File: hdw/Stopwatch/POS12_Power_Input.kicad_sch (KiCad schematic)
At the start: 19 parts, among them J201 +12V IN, U201 TPS26600RHFT

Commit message: started sch work
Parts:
- removed C202: 10nF, Capacitors_SMD:C_0603, symbol Custom_Library:C_Custom
- removed C203: 1nF, Capacitors_SMD:C_0603, symbol Custom_Library:C_Custom
- D201: Config (none) -> DNP
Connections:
- net at U201.12 (OVP): now also R?.1, R?.2
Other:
- moved on the sheet: C201, C204, C205, D201, J201, R?, TP201, TP203

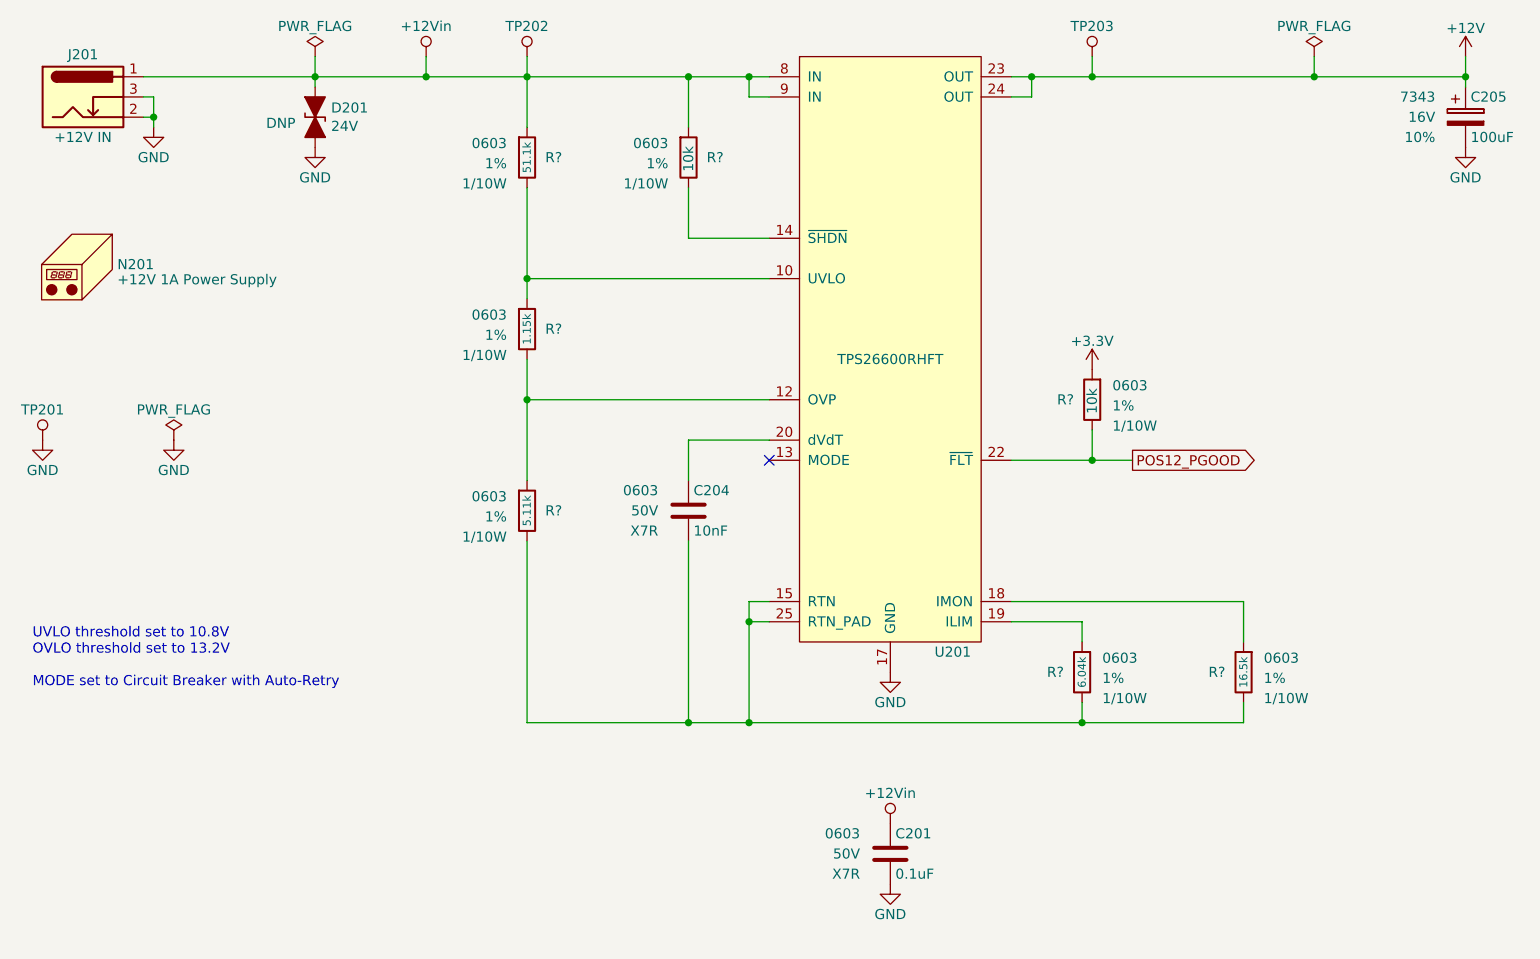
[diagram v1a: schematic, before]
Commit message: adjusted stage sheet
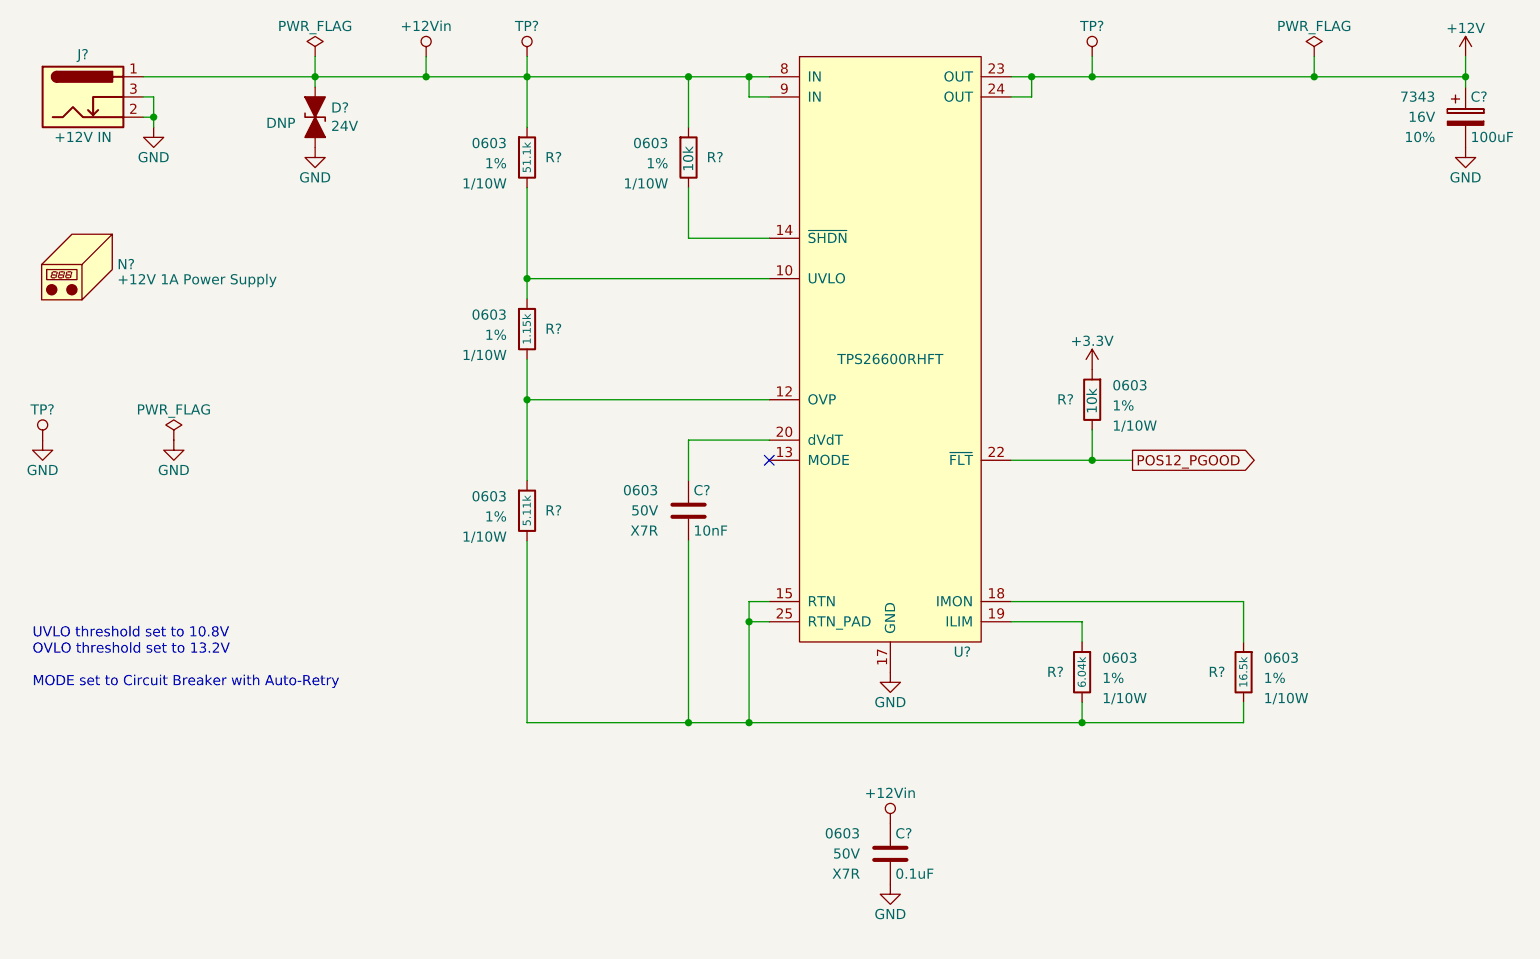
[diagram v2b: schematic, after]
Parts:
- renumbered C201 to C?, C205 to C?, C204 to C?, D201 to D?, J201 to J?, N201 to N?, TP203 to TP?, TP202 to TP?, TP201 to TP?, U201 to U?
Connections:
- net at U?.12 (OVP): now also R?.1, R?.2

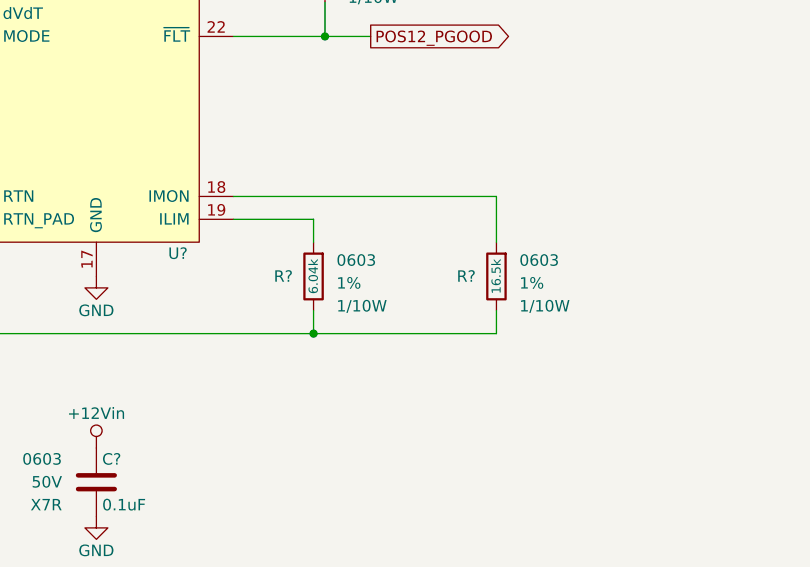
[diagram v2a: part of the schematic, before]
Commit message: added reset stuff
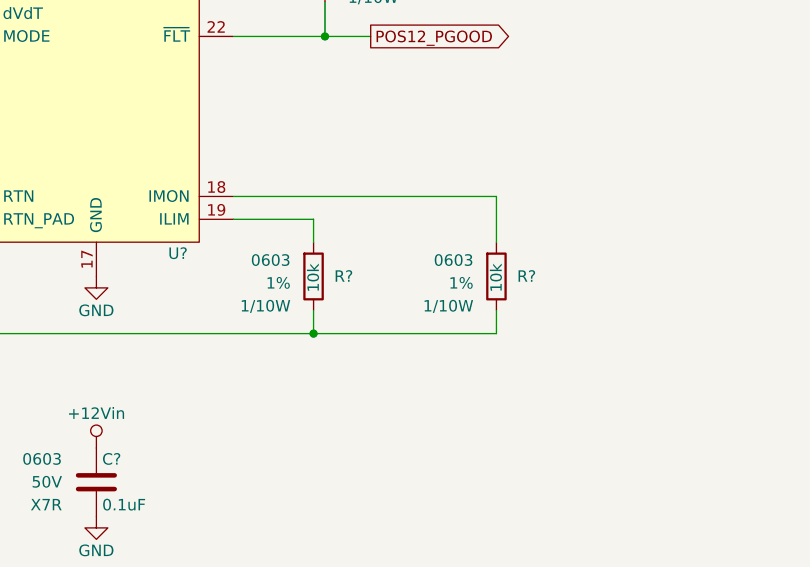
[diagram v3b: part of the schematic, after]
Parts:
- removed R?: 6.04k, Resistors_SMD:R_0603, symbol Custom_Library:R_Custom
- removed R?: 16.5k, Resistors_SMD:R_0603, symbol Custom_Library:R_Custom
- added R? (x2): 10k, Resistors_SMD:R_0603, symbol Custom_Library:R_Custom
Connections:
- net at U?.12 (OVP): now also R?.1, R?.2
- net at C?.2, R?.2, U?.15 (RTN)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: now also R?.2, R?.2
- net at U?.18 (IMON): now also R?.1
- net at U?.19 (ILIM): now also R?.1
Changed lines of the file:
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@@
-    )
-  )
-  (symbol (lib_id "Custom_Library:R_Custom") (at 166.37 132.08 0) (unit 1)
-    (in_bom yes) (on_board yes) (dnp no)
-    (property "Reference" "R?" (at 164.084 132.08 0)
-      (effects (font (size 1.27 1.27)) (justify right))
-    )
-    (property "Value" "6.04k" (at 166.37 132.08 90)
-      (effects (font (size 1.016 1.016)))
-    )
-    (property "Footprint" "Resistors_SMD:R_0603" (at 166.37 132.08 0)
-      (effects (font (size 1.27 1.27)) hide)
-    )
-    (property "Datasheet" "" (at 166.37 132.08 0)
-      (effects (font (size 1.27 1.27)) hide)
-    )
-    (property "display_footprint" "0603" (at 168.91 130.302 0)
-      (effects (font (size 1.27 1.27)) (justify left))
-    )
-    (property "Tolerance" "1%" (at 168.91 132.842 0)
-      (effects (font (size 1.27 1.27)) (justify left))
-    )
-    (property "Wattage" "1/10W" (at 168.91 135.382 0)
-      (effects (font (size 1.27 1.27)) (justify left))
-    )
-    (property "Digi-Key PN" "RMCF0603FT10K0CT-ND" (at 173.99 121.92 0)
-      (effects (font (size 1.524 1.524)) hide)
-    )
-    (pin "1")
-    (pin "2")
-    (instances
-      (project "Stopwatch"
-        (path "/c0d2575b-aec2-49ed-8c32-97fe6e68824c/00000000-0000-0000-0000-00005d6c0d23"
-          (reference "R?") (unit 1)
-        )
-        (path "/c0d2575b-aec2-49ed-8c32-97fe6e68824c/00000000-0000-0000-0000-00005d6b2673"
-          (reference "R?") (unit 1)
-        )
-        (path "/c0d2575b-aec2-49ed-8c32-97fe6e68824c/00000000-0000-0000-0000-00005d77a516"
-          (reference "R?") (unit 1)
-        )
-      )
-    )
-  )
-  (symbol (lib_id "Custom_Library:R_Custom") (at 186.69 132.08 0) (unit 1)
-    (in_bom yes) (on_board yes) (dnp no)
-    (property "Reference" "R?" (at 184.404 132.08 0)
-      (effects (font (size 1.27 1.27)) (justify right))
-    )
-    (property "Value" "16.5k" (at 186.69 132.08 90)
-      (effects (font (size 1.016 1.016)))
-    )
-    (property "Footprint" "Resistors_SMD:R_0603" (at 186.69 132.08 0)
-      (effects (font (size 1.27 1.27)) hide)
-    )
-    (property "Datasheet" "" (at 186.69 132.08 0)
-      (effects (font (size 1.27 1.27)) hide)
-    )
-    (property "display_footprint" "0603" (at 189.23 130.302 0)
-      (effects (font (size 1.27 1.27)) (justify left))
-    )
-    (property "Tolerance" "1%" (at 189.23 132.842 0)
-      (effects (font (size 1.27 1.27)) (justify left))
-    )
-    (property "Wattage" "1/10W" (at 189.23 135.382 0)
-      (effects (font (size 1.27 1.27)) (justify left))
-    )
-    (property "Digi-Key PN" "RMCF0603FT10K0CT-ND" (at 194.31 121.92 0)
-      (effects (font (size 1.524 1.524)) hide)
-    )
-    (pin "1")
-    (pin "2")
-    (instances
-      (project "Stopwatch"
-        (path "/c0d2575b-aec2-49ed-8c32-97fe6e68824c/00000000-0000-0000-0000-00005d6c0d23"
-          (reference "R?") (unit 1)
-        )
-        (path "/c0d2575b-aec2-49ed-8c32-97fe6e68824c/00000000-0000-0000-0000-00005d6b2673"
-          (reference "R?") (unit 1)
-        )
-        (path "/c0d2575b-aec2-49ed-8c32-97fe6e68824c/00000000-0000-0000-0000-00005d77a516"
-          (reference "R?") (unit 1)
-        )
-      )
     )
   )
@@
         )
       )
+    )
+  )
+  (symbol (lib_id "Custom_Library:R_Custom") (at 186.69 132.08 0) (mirror y) (unit 1)
+    (in_bom yes) (on_board yes) (dnp no)
+    (property "Reference" "R?" (at 188.976 132.08 0)
+      (effects (font (size 1.27 1.27)) (justify right))
+    )
+    (property "Value" "10k" (at 186.69 133.858 90)
+      (effects (font (size 1.27 1.27)) (justify left))
+    )
+    (property "Footprint" "Resistors_SMD:R_0603" (at 186.69 132.08 0)
+      (effects (font (size 1.27 1.27)) hide)
+    )
+    (property "Datasheet" "" (at 186.69 132.08 0)
+      (effects (font (size 1.27 1.27)) hide)
+    )
+    (property "display_footprint" "0603" (at 184.15 130.302 0)
+      (effects (font (size 1.27 1.27)) (justify left))
+    )
+    (property "Tolerance" "1%" (at 184.15 132.842 0)
+      (effects (font (size 1.27 1.27)) (justify left))
+    )
+    (property "Wattage" "1/10W" (at 184.15 135.382 0)
+      (effects (font (size 1.27 1.27)) (justify left))
+    )
+    (property "Digi-Key PN" "RMCF0603FT10K0CT-ND" (at 179.07 121.92 0)
+      (effects (font (size 1.524 1.524)) hide)
+    )
+    (pin "1")
+    (pin "2")
+    (instances
+      (project "Stopwatch"
+        (path "/c0d2575b-aec2-49ed-8c32-97fe6e68824c/00000000-0000-0000-0000-00005d6c0d23"
+          (reference "R?") (unit 1)
+        )
+        (path "/c0d2575b-aec2-49ed-8c32-97fe6e68824c/00000000-0000-0000-0000-00005d6b2673"
+          (reference "R?") (unit 1)
+        )
+        (path "/c0d2575b-aec2-49ed-8c32-97fe6e68824c/00000000-0000-0000-0000-00005d77a516"
+          (reference "R?") (unit 1)
+        )
+      )
+    )
+  )
+  (symbol (lib_id "Custom_Library:R_Custom") (at 166.37 132.08 0) (mirror y) (unit 1)
+    (in_bom yes) (on_board yes) (dnp no)
+    (property "Reference" "R?" (at 168.656 132.08 0)
+      (effects (font (size 1.27 1.27)) (justify right))
+    )
+    (property "Value" "10k" (at 166.37 133.858 90)
+      (effects (font (size 1.27 1.27)) (justify left))
+    )
+    (property "Footprint" "Resistors_SMD:R_0603" (at 166.37 132.08 0)
+      (effects (font (size 1.27 1.27)) hide)
+    )
+    (property "Datasheet" "" (at 166.37 132.08 0)
+      (effects (font (size 1.27 1.27)) hide)
+    )
+    (property "display_footprint" "0603" (at 163.83 130.302 0)
+      (effects (font (size 1.27 1.27)) (justify left))
+    )
+    (property "Tolerance" "1%" (at 163.83 132.842 0)
+      (effects (font (size 1.27 1.27)) (justify left))
+    )
+    (property "Wattage" "1/10W" (at 163.83 135.382 0)
+      (effects (font (size 1.27 1.27)) (justify left))
+    )
+    (property "Digi-Key PN" "RMCF0603FT10K0CT-ND" (at 158.75 121.92 0)
+      (effects (font (size 1.524 1.524)) hide)
+    )
+    (pin "1")
+    (pin "2")
+    (instances
+      (project "Stopwatch"
+        (path "/c0d2575b-aec2-49ed-8c32-97fe6e68824c/00000000-0000-0000-0000-00005d6c0d23"
+          (reference "R?") (unit 1)
+        )
+        (path "/c0d2575b-aec2-49ed-8c32-97fe6e68824c/00000000-0000-0000-0000-00005d6b2673"
+          (reference "R?") (unit 1)
+        )
+        (path "/c0d2575b-aec2-49ed-8c32-97fe6e68824c/00000000-0000-0000-0000-00005d77a516"
+          (reference "R?") (unit 1)
+        )
+      )

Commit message: added more reset stuff
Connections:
- net at U?.12 (OVP): now also R?.1, R?.2

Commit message: copied to minutes reset sheet
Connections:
- net at U?.12 (OVP): now also R?.1, R?.2

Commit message: added some more junk
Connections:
- net at U?.12 (OVP): now also R?.1, R?.2
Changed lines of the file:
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@@
   (title_block
     (title "Stopwatch")
-    (date "2024-01-02")
+    (date "2024-01-11")
     (rev "A")
     (company "Drew Maatman")

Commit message: reordered schematic sheets
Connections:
- net at U?.12 (OVP): now also R?.1, R?.2
